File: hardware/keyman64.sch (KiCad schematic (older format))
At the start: 28 parts, among them IC1 ATMEGA1284P-P, P1 TAPEPORT, P2 CIA1, P3 KEYBOARD, P4 USER, P6 USB, SW1 RESET, SW2 BOOTLOADER, U1 7400, U2 ICL7660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

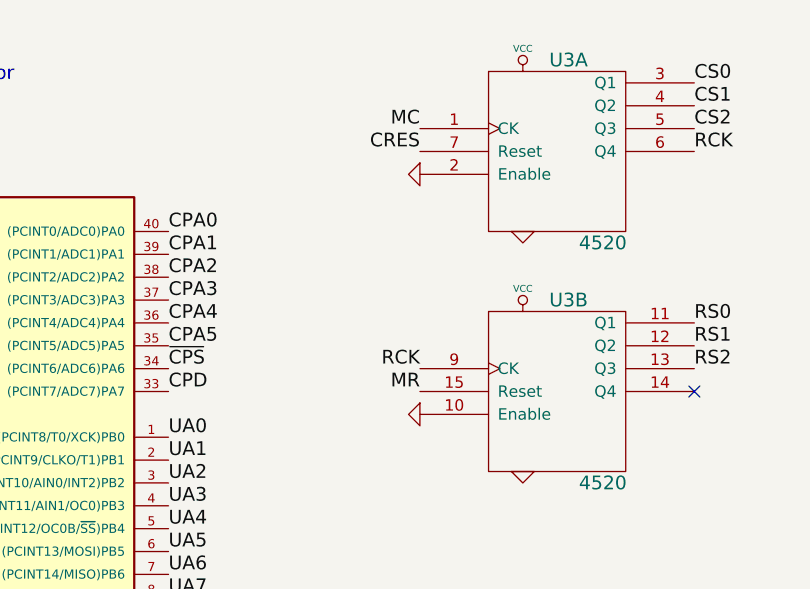
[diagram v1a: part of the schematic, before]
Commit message: Hardware: Fixed bug in schematics/pcb (4520 enable to VCC)
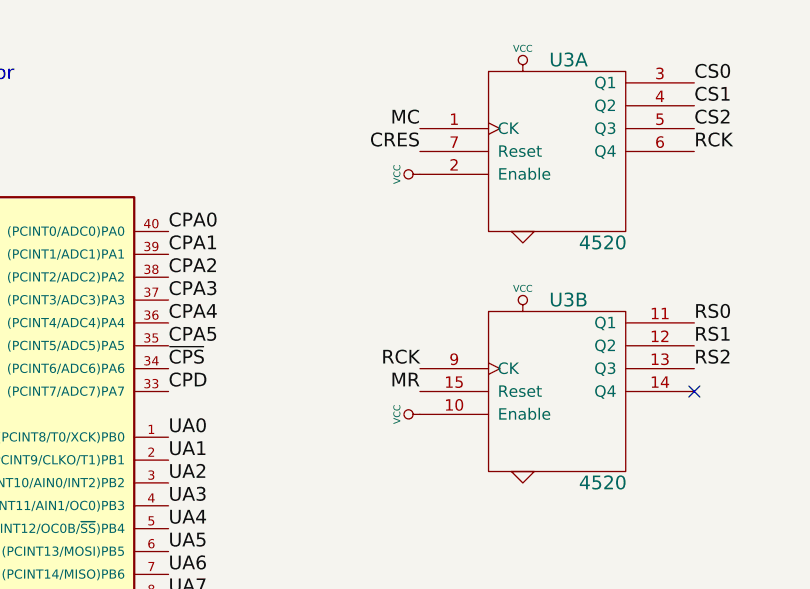
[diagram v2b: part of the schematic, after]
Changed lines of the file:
@@
 LIBS:cd74hc22106
 LIBS:keyman64-cache
-EELAYER 27 0
+EELAYER 24 0
 EELAYER END
 $Descr A4 11693 8268
@@
 Text Label 5400 4500 2    60   ~ 0
 RCK
-$Comp
-L GND #PWR09
-U 1 1 55A76DEF
-P 5400 3650
-F 0 "#PWR09" H 5400 3650 30  0001 C CNN
-F 1 "GND" H 5400 3580 30  0001 C CNN
-F 2 "" H 5400 3650 60  0000 C CNN
-F 3 "" H 5400 3650 60  0000 C CNN
-	1    5400 3650
-	0    1    1    0
-$EndComp
-$Comp
-L GND #PWR010
-U 1 1 55A76DFE
-P 5400 4700
-F 0 "#PWR010" H 5400 4700 30  0001 C CNN
-F 1 "GND" H 5400 4630 30  0001 C CNN
-F 2 "" H 5400 4700 60  0000 C CNN
-F 3 "" H 5400 4700 60  0000 C CNN
-	1    5400 4700
-	0    1    1    0
-$EndComp
 Text Label 4950 1850 2    60   ~ 0
 RCK
@@
 Text Label 1800 3150 2    60   ~ 0
 EXTVCC
+$Comp
+L VCC #PWR?
+U 1 1 55D17350
+P 5400 4700
+F 0 "#PWR?" H 5400 4800 30  0001 C CNN
+F 1 "VCC" H 5400 4800 30  0000 C CNN
+F 2 "" H 5400 4700 60  0000 C CNN
+F 3 "" H 5400 4700 60  0000 C CNN
+	1    5400 4700
+	0    -1   -1   0
+$EndComp
+$Comp
+L VCC #PWR?
+U 1 1 55D17362
+P 5400 3650
+F 0 "#PWR?" H 5400 3750 30  0001 C CNN
+F 1 "VCC" H 5400 3750 30  0000 C CNN
+F 2 "" H 5400 3650 60  0000 C CNN
+F 3 "" H 5400 3650 60  0000 C CNN
+	1    5400 3650
+	0    -1   -1   0
+$EndComp
 $EndSCHEMATC

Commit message: Hardware: Removed EXTVCC Jumper, removed copper around edges
There is no VCC on the keyboard connector, so VCC must be fed from external
source anyways if the keyboard cable is simply cut in half and the board
soldered in between.

The copper/traces around the keyboard/cia connectors have been removed to
make it easier to simply solder the wires in instead of adding pin headers
and proper plugs.
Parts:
- removed JP1: JUMPER, ~, symbol JUMPER
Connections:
- net labels removed: EXTVCC
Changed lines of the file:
@@
 LIBS:cd74hc22106
 LIBS:keyman64-cache
-EELAYER 24 0
+EELAYER 27 0
 EELAYER END
 $Descr A4 11693 8268
@@
 Sheet 1 1
 Title "Programmable C64 Keyboard Interceptor and Controller"
-Date "15 aug 2015"
+Date "18 aug 2015"
 Rev "1"
 Comp "Henning Bekel"
@@
 Text Label 900  4550 2    60   ~ 0
 A7
-Text Label 2400 3150 0    60   ~ 0
+Text Label 900  2950 2    60   ~ 0
 VCC
 Text Label 4050 1100 0    60   ~ 0
@@
 MD
 $Comp
-L GND #PWR011
+L GND #PWR09
 U 1 1 55A77078
 P 8900 2650
-F 0 "#PWR011" H 8900 2650 30  0001 C CNN
+F 0 "#PWR09" H 8900 2650 30  0001 C CNN
 F 1 "GND" H 8900 2580 30  0001 C CNN
 F 2 "" H 8900 2650 60  0000 C CNN
@@
 $EndComp
 $Comp
-L GND #PWR012
+L GND #PWR010
 U 1 1 55A772ED
 P 9500 2250
-F 0 "#PWR012" H 9500 2250 30  0001 C CNN
+F 0 "#PWR010" H 9500 2250 30  0001 C CNN
 F 1 "GND" H 9500 2180 30  0001 C CNN
 F 2 "" H 9500 2250 60  0000 C CNN
@@
 $EndComp
 $Comp
-L VCC #PWR013
+L VCC #PWR011
 U 1 1 55A772FC
 P 9500 950
-F 0 "#PWR013" H 9500 1050 30  0001 C CNN
+F 0 "#PWR011" H 9500 1050 30  0001 C CNN
 F 1 "VCC" H 9500 1050 30  0000 C CNN
 F 2 "" H 9500 950 60  0000 C CNN
@@
 VEE
 $Comp
-L GND #PWR014
+L GND #PWR012
 U 1 1 55A77382
 P 10650 1850
-F 0 "#PWR014" H 10650 1850 30  0001 C CNN
+F 0 "#PWR012" H 10650 1850 30  0001 C CNN
 F 1 "GND" H 10650 1780 30  0001 C CNN
 F 2 "" H 10650 1850 60  0000 C CNN
@@
 $EndComp
 $Comp
-L GND #PWR015
+L GND #PWR013
 U 1 1 55A774B7
 P 7500 5100
-F 0 "#PWR015" H 7500 5100 30  0001 C CNN
+F 0 "#PWR013" H 7500 5100 30  0001 C CNN
 F 1 "GND" H 7500 5030 30  0001 C CNN
 F 2 "" H 7500 5100 60  0000 C CNN
@@
 $EndComp
 $Comp
-L GND #PWR016
+L GND #PWR014
 U 1 1 55A774BD
 P 7500 3550
-F 0 "#PWR016" H 7500 3550 30  0001 C CNN
+F 0 "#PWR014" H 7500 3550 30  0001 C CNN
 F 1 "GND" H 7500 3480 30  0001 C CNN
 F 2 "" H 7500 3550 60  0000 C CNN
@@
 Connection ~ 2050 4800
 $Comp
-L GND #PWR017
+L GND #PWR015
 U 1 1 55A77919
 P 1900 5200
-F 0 "#PWR017" H 1900 5200 30  0001 C CNN
+F 0 "#PWR015" H 1900 5200 30  0001 C CNN
 F 1 "GND" H 1900 5130 30  0001 C CNN
 F 2 "" H 1900 5200 60  0000 C CNN
@@
 $EndComp
 $Comp
-L GND #PWR018
+L GND #PWR016
 U 1 1 55A77928
 P 1900 3800
-F 0 "#PWR018" H 1900 3800 30  0001 C CNN
+F 0 "#PWR016" H 1900 3800 30  0001 C CNN
 F 1 "GND" H 1900 3730 30  0001 C CNN
 F 2 "" H 1900 3800 60  0000 C CNN
@@
 $EndComp
 $Comp
-L VCC #PWR019
+L VCC #PWR017
 U 1 1 55A77A74
 P 5850 3200
-F 0 "#PWR019" H 5850 3300 30  0001 C CNN
+F 0 "#PWR017" H 5850 3300 30  0001 C CNN
 F 1 "VCC" H 5850 3300 30  0000 C CNN
 F 2 "" H 5850 3200 60  0000 C CNN
@@
 $EndComp
 $Comp
-L VCC #PWR020
+L VCC #PWR018
 U 1 1 55A77A8E
 P 5850 4250
-F 0 "#PWR020" H 5850 4350 30  0001 C CNN
+F 0 "#PWR018" H 5850 4350 30  0001 C CNN
 F 1 "VCC" H 5850 4350 30  0000 C CNN
 F 2 "" H 5850 4250 60  0000 C CNN
@@
 $EndComp
 $Comp
-L VCC #PWR021
+L VCC #PWR019
 U 1 1 55A77A94
 P 8200 2600
-F 0 "#PWR021" H 8200 2700 30  0001 C CNN
+F 0 "#PWR019" H 8200 2700 30  0001 C CNN
 F 1 "VCC" H 8200 2700 30  0000 C CNN
 F 2 "" H 8200 2600 60  0000 C CNN
@@
 $EndComp
 $Comp
-L VCC #PWR022
+L VCC #PWR020
 U 1 1 55A77A9A
 P 8200 4150
-F 0 "#PWR022" H 8200 4250 30  0001 C CNN
+F 0 "#PWR020" H 8200 4250 30  0001 C CNN
 F 1 "VCC" H 8200 4250 30  0000 C CNN
 F 2 "" H 8200 4150 60  0000 C CNN
@@
 $EndComp
 $Comp
-L GND #PWR023
+L GND #PWR021
 U 1 1 55A77AA2
 P 5850 3900
-F 0 "#PWR023" H 5850 3900 30  0001 C CNN
+F 0 "#PWR021" H 5850 3900 30  0001 C CNN
 F 1 "GND" H 5850 3830 30  0001 C CNN
 F 2 "" H 5850 3900 60  0000 C CNN
@@
 $EndComp
 $Comp
-L GND #PWR024
+L GND #PWR022
 U 1 1 55A77AAF
 P 5850 4950
-F 0 "#PWR024" H 5850 4950 30  0001 C CNN
+F 0 "#PWR022" H 5850 4950 30  0001 C CNN
 F 1 "GND" H 5850 4880 30  0001 C CNN
 F 2 "" H 5850 4950 60  0000 C CNN
@@
 $EndComp
 $Comp
-L GND #PWR025
+L GND #PWR023
 U 1 1 55A77AB5
 P 8200 3900
-F 0 "#PWR025" H 8200 3900 30  0001 C CNN
+F 0 "#PWR023" H 8200 3900 30  0001 C CNN
 F 1 "GND" H 8200 3830 30  0001 C CNN
 F 2 "" H 8200 3900 60  0000 C CNN
@@
 $EndComp
 $Comp
-L GND #PWR026
+L GND #PWR024
 U 1 1 55A77ABB
 P 8200 5450
-F 0 "#PWR026" H 8200 5450 30  0001 C CNN
+F 0 "#PWR024" H 8200 5450 30  0001 C CNN
 F 1 "GND" H 8200 5380 30  0001 C CNN
 F 2 "" H 8200 5450 60  0000 C CNN
@@
 $EndComp
 $Comp
-L VCC #PWR027
+L VCC #PWR025
 U 1 1 55A77F84
 P 10200 5650
-F 0 "#PWR027" H 10200 5750 30  0001 C CNN
+F 0 "#PWR025" H 10200 5750 30  0001 C CNN
 F 1 "VCC" H 10200 5750 30  0000 C CNN
 F 2 "" H 10200 5650 60  0000 C CNN
@@
 $EndComp
 $Comp
-L GND #PWR028
+L GND #PWR026
 U 1 1 55A77F8A
 P 10200 6050
-F 0 "#PWR028" H 10200 6050 30  0001 C CNN
+F 0 "#PWR026" H 10200 6050 30  0001 C CNN
 F 1 "GND" H 10200 5980 30  0001 C CNN
 F 2 "" H 10200 6050 60  0000 C CNN
@@
 $EndComp
 $Comp
-L VCC #PWR029
+L VCC #PWR027
 U 1 1 55A77F96
 P 10450 5650
-F 0 "#PWR029" H 10450 5750 30  0001 C CNN
+F 0 "#PWR027" H 10450 5750 30  0001 C CNN
 F 1 "VCC" H 10450 5750 30  0000 C CNN
 F 2 "" H 10450 5650 60  0000 C CNN
@@
 $EndComp
 $Comp
-L GND #PWR030
+L GND #PWR028
 U 1 1 55A77F9C
 P 10450 6050
-F 0 "#PWR030" H 10450 6050 30  0001 C CNN
+F 0 "#PWR028" H 10450 6050 30  0001 C CNN
 F 1 "GND" H 10450 5980 30  0001 C CNN
 F 2 "" H 10450 6050 60  0000 C CNN
@@
 $EndComp
 $Comp
-L VCC #PWR031
+L VCC #PWR029
 U 1 1 55A77FA8
 P 10700 5650
-F 0 "#PWR031" H 10700 5750 30  0001 C CNN
+F 0 "#PWR029" H 10700 5750 30  0001 C CNN
 F 1 "VCC" H 10700 5750 30  0000 C CNN
 F 2 "" H 10700 5650 60  0000 C CNN
@@
 $EndComp
 $Comp
-L GND #PWR032
+L GND #PWR030
 U 1 1 55A77FAE
 P 10700 6050
-F 0 "#PWR032" H 10700 6050 30  0001 C CNN
+F 0 "#PWR030" H 10700 6050 30  0001 C CNN
 F 1 "GND" H 10700 5980 30  0001 C CNN
 F 2 "" H 10700 6050 60  0000 C CNN
@@
 VEE
 $Comp
-L GND #PWR033
+L GND #PWR031
 U 1 1 55B35D41
 P 8900 5300
-F 0 "#PWR033" H 8900 5300 30  0001 C CNN
+F 0 "#PWR031" H 8900 5300 30  0001 C CNN
 F 1 "GND" H 8900 5230 30  0001 C CNN
 F 2 "" H 8900 5300 60  0000 C CNN
@@
 $EndComp
 $Comp
-L VCC #PWR034
+L VCC #PWR032
 U 1 1 55B37587
 P 3350 1050
-F 0 "#PWR034" H 3350 1150 30  0001 C CNN
+F 0 "#PWR032" H 3350 1150 30  0001 C CNN
 F 1 "VCC" H 3350 1150 30  0000 C CNN
 F 2 "" H 3350 1050 60  0000 C CNN
@@
 CPD
 $Comp
-L GND #PWR035
+L GND #PWR033
 U 1 1 55B37A62
 P 7150 6600
-F 0 "#PWR035" H 7150 6600 30  0001 C CNN
+F 0 "#PWR033" H 7150 6600 30  0001 C CNN
 F 1 "GND" H 7150 6530 30  0001 C CNN
 F 2 "" H 7150 6600 60  0000 C CNN
@@
 $EndComp
 $Comp
-L GND #PWR036
+L GND #PWR034
 U 1 1 55B37A96
 P 7150 6250
-F 0 "#PWR036" H 7150 6250 30  0001 C CNN
+F 0 "#PWR034" H 7150 6250 30  0001 C CNN
 F 1 "GND" H 7150 6180 30  0001 C CNN
 F 2 "" H 7150 6250 60  0000 C CNN
@@
 $EndComp
 $Comp
-L VCC #PWR037
+L VCC #PWR035
 U 1 1 55B387FF
 P 5200 6200
-F 0 "#PWR037" H 5200 6300 30  0001 C CNN
+F 0 "#PWR035" H 5200 6300 30  0001 C CNN
 F 1 "VCC" H 5200 6300 30  0000 C CNN
 F 2 "" H 5200 6200 60  0000 C CNN
@@
 $EndComp
 $Comp
-L GND #PWR038
+L GND #PWR036
 U 1 1 55B38813
 P 5200 7200
-F 0 "#PWR038" H 5200 7200 30  0001 C CNN
+F 0 "#PWR036" H 5200 7200 30  0001 C CNN
 F 1 "GND" H 5200 7130 30  0001 C CNN
 F 2 "" H 5200 7200 60  0000 C CNN
@@
 $EndComp
 $Comp
-L GND #PWR039
+L GND #PWR037
 U 1 1 55B38825
 P 4900 7100
-F 0 "#PWR039" H 4900 7100 30  0001 C CNN
+F 0 "#PWR037" H 4900 7100 30  0001 C CNN
 F 1 "GND" H 4900 7030 30  0001 C CNN
 F 2 "" H 4900 7100 60  0000 C CNN
@@
 NoConn ~ 11000 6750
 $Comp
-L GND #PWR040
+L GND #PWR038
 U 1 1 55B4B074
 P 9800 6650
-F 0 "#PWR040" H 9800 6650 30  0001 C CNN
+F 0 "#PWR038" H 9800 6650 30  0001 C CNN
 F 1 "GND" H 9800 6580 30  0001 C CNN
 F 2 "" H 9800 6650 60  0000 C CNN
@@
 $EndComp
 $Comp
-L GND #PWR041
+L GND #PWR039
 U 1 1 55B4B08B
 P 9800 6850
-F 0 "#PWR041" H 9800 6850 30  0001 C CNN
+F 0 "#PWR039" H 9800 6850 30  0001 C CNN
 F 1 "GND" H 9800 6780 30  0001 C CNN
 F 2 "" H 9800 6850 60  0000 C CNN
@@
 MR
 $Comp
-L GND #PWR042
+L GND #PWR040
 U 1 1 55B68DDD
 P 2650 2700
-F 0 "#PWR042" H 2650 2700 30  0001 C CNN
+F 0 "#PWR040" H 2650 2700 30  0001 C CNN
 F 1 "GND" H 2650 2630 30  0001 C CNN
 F 2 "" H 2650 2700 60  0000 C CNN
@@
 ~CPMR
 $Comp
-L GND #PWR043
+L GND #PWR041
 U 1 1 55BD089A
 P 3350 2750
-F 0 "#PWR043" H 3350 2750 30  0001 C CNN
+F 0 "#PWR041" H 3350 2750 30  0001 C CNN
 F 1 "GND" H 3350 2680 30  0001 C CNN
 F 2 "" H 3350 2750 60  0000 C CNN
@@
 D+
 $Comp
-L GND #PWR044
+L GND #PWR042
 U 1 1 55BF10BD
 P 900 2050
-F 0 "#PWR044" H 900 2050 30  0001 C CNN
+F 0 "#PWR042" H 900 2050 30  0001 C CNN
 F 1 "GND" H 900 1980 30  0001 C CNN
 F 2 "" H 900 2050 60  0000 C CNN
@@
 Text Notes 10050 5400 0    60   ~ 0
 Stabilizing caps
-Text Label 900  2950 2    60   ~ 0
-EXTVCC
-$Comp
-L JUMPER JP1
-U 1 1 55BF8D49
-P 2100 3150
-F 0 "JP1" H 2100 3300 60  0000 C CNN
-F 1 "JUMPER" H 2100 3070 40  0000 C CNN
-F 2 "~" H 2100 3150 60  0000 C CNN
-F 3 "~" H 2100 3150 60  0000 C CNN
-	1    2100 3150
-	1    0    0    -1
-$EndComp
-Text Label 1800 3150 2    60   ~ 0
-EXTVCC
-$Comp
-L VCC #PWR?
+$Comp
+L VCC #PWR043
 U 1 1 55D17350
 P 5400 4700
-F 0 "#PWR?" H 5400 4800 30  0001 C CNN
+F 0 "#PWR043" H 5400 4800 30  0001 C CNN
 F 1 "VCC" H 5400 4800 30  0000 C CNN
 F 2 "" H 5400 4700 60  0000 C CNN
@@
 $EndComp
 $Comp
-L VCC #PWR?
+L VCC #PWR044
 U 1 1 55D17362
 P 5400 3650
-F 0 "#PWR?" H 5400 3750 30  0001 C CNN
+F 0 "#PWR044" H 5400 3750 30  0001 C CNN
 F 1 "VCC" H 5400 3750 30  0000 C CNN
 F 2 "" H 5400 3650 60  0000 C CNN

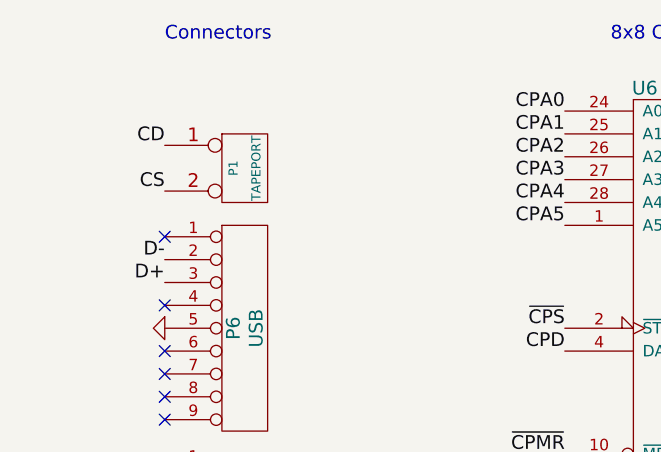
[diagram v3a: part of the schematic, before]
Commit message: Hardware: Moved values and refs on pcb, added svg renderings
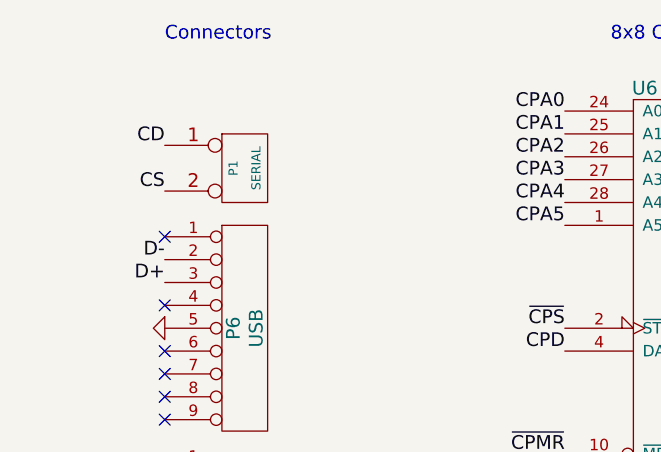
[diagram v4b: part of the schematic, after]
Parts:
- P1: value TAPEPORT -> SERIAL
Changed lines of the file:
@@
 Sheet 1 1
 Title "Programmable C64 Keyboard Interceptor and Controller"
-Date "18 aug 2015"
+Date "1 oct 2015"
 Rev "1"
 Comp "Henning Bekel"
@@
 P 1250 1350
 F 0 "P1" V 1200 1350 40  0000 C CNN
-F 1 "TAPEPORT" V 1300 1350 40  0000 C CNN
+F 1 "SERIAL" V 1300 1350 40  0000 C CNN
 F 2 "" H 1250 1350 60  0000 C CNN
 F 3 "" H 1250 1350 60  0000 C CNN

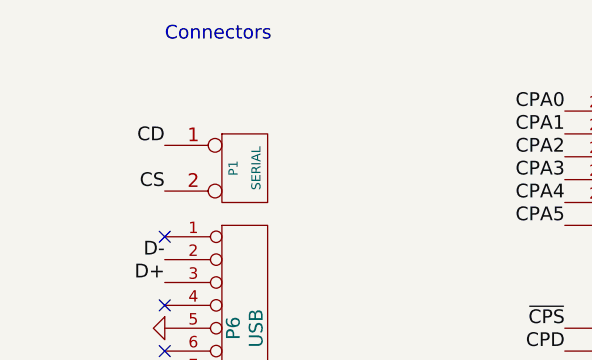
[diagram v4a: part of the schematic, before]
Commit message: Hardware: Rev.2, Increased VIA sizes, Added alternative VCC pin header
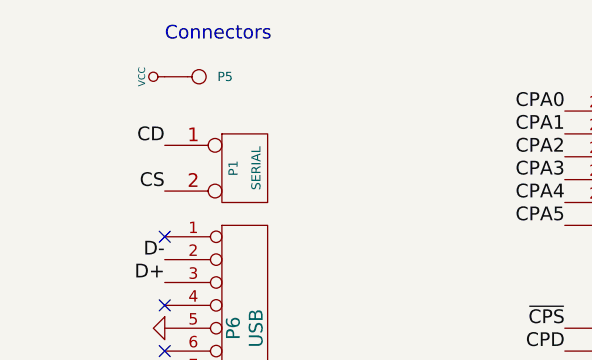
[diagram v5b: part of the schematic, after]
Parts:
- added P5: POWER, symbol CONN_1
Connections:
- net VCC: now also P5.1
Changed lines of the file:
@@
 encoding utf-8
 Sheet 1 1
-Title "Programmable C64 Keyboard Interceptor and Controller"
-Date "1 oct 2015"
-Rev "1"
+Title "Programmable C64 Keyboard Interceptor and Hardware Controller"
+Date "14 oct 2015"
+Rev "2"
 Comp "Henning Bekel"
 Comment1 ""
@@
 	0    -1   -1   0
 $EndComp
+$Comp
+L CONN_1 P5
+U 1 1 561E3336
+P 1050 950
+F 0 "P5" H 1130 950 40  0000 L CNN
+F 1 "POWER" H 1050 1005 30  0001 C CNN
+F 2 "" H 1050 950 60  0000 C CNN
+F 3 "" H 1050 950 60  0000 C CNN
+	1    1050 950
+	1    0    0    -1
+$EndComp
+$Comp
+L VCC #PWR045
+U 1 1 561E3345
+P 900 950
+F 0 "#PWR045" H 900 1050 30  0001 C CNN
+F 1 "VCC" H 900 1050 30  0000 C CNN
+F 2 "" H 900 950 60  0000 C CNN
+F 3 "" H 900 950 60  0000 C CNN
+	1    900  950
+	0    -1   -1   0
+$EndComp

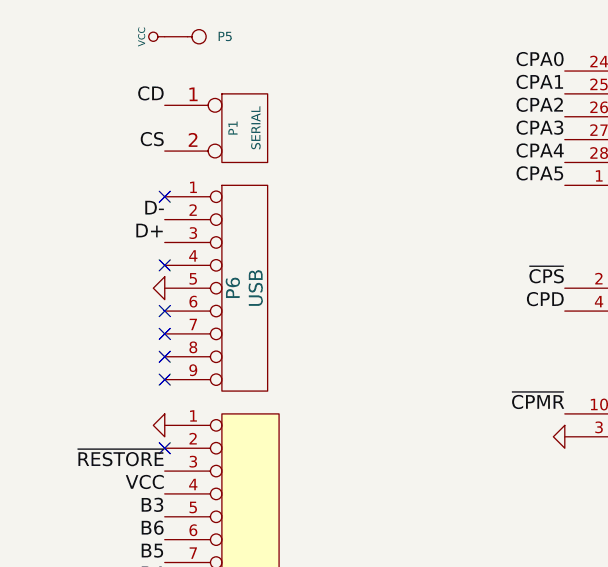
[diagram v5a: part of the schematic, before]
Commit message: Hardware: Changed USB connector to mini-usb-b through-hole footprint
The footprints fit has not been verified yet, it was created based on the
datasheet for the reichelt part "USB BWM".
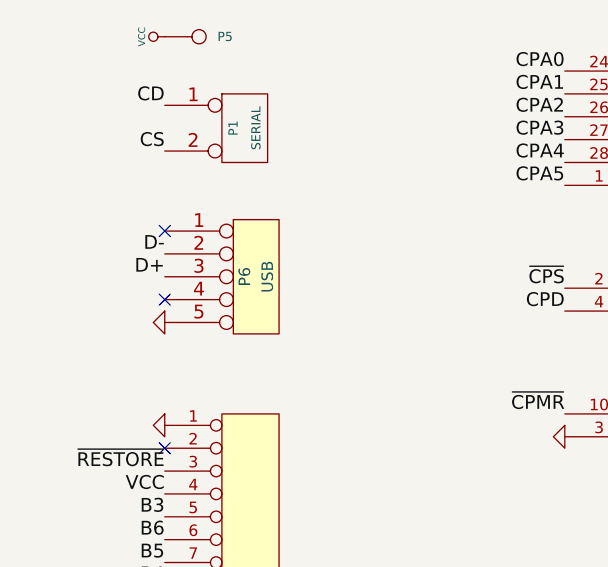
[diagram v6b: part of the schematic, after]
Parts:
- removed P6: USB, symbol CONN_9
- added P6: USB, symbol CONN_5
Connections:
- net D+: now also P6.3
- net D-: now also P6.2
- net GND: now also P6.5
- no-connect marks 13 -> 9

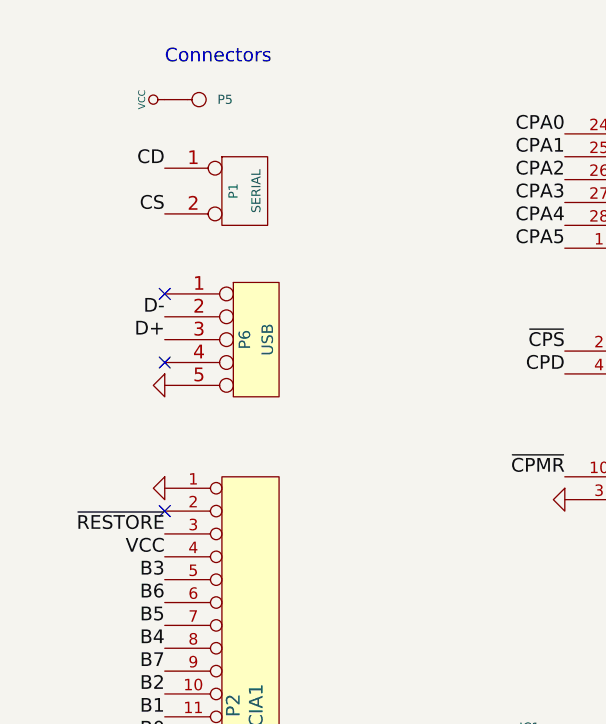
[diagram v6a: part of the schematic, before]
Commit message: Hardware: Added option to power device from USB or external source
This makes it easier to use the device as a standalone keyboard controller,
i.e. without actually connecting it to a computer.

The software will support a standalone mode, in which no crosspoint switch
and consequently no meta key is required. The port used for the crosspoint
switch control will be made available as an additional user control port.
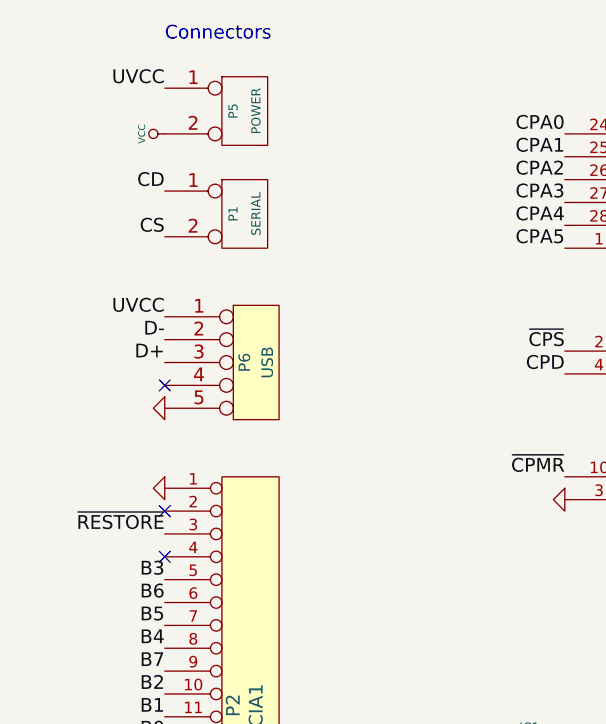
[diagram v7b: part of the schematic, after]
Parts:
- removed P5: POWER, symbol CONN_1
- added P5: POWER, symbol CONN_2
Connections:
- net VCC: now also P5.2 (PM); no longer P2.4 (P4)
- net UVCC: now reaches P6.1
- net UVCC: now also P5.1 (P1)
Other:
- moved on the sheet: P1, P6
